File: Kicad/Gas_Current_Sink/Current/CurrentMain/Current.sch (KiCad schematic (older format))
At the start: 18 parts, among them J1 Vo's, J2 ACS770, J3 ACS712, J4 PA3208, J5 SCT, J6 Current

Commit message: Kicad Current project update Kicad TH project update
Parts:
- removed J2: ACS770, symbol CONN_01X05
- removed J3: ACS712, symbol CONN_01X05
- removed J6: Current, symbol CONN_01X02
- added J?: ACS770, symbol CONN_01X03
- added J?: ACS712, symbol CONN_01X03
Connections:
- net labels removed: IP+
- wire segments 58 -> 49
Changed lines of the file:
@@
-$EndComp
-$Comp
-L CONN_01X05 J2
-U 1 1 59DBFBDD
-P 1650 1200
-F 0 "J2" H 1650 1500 50  0000 C CNN
-F 1 "ACS770" V 1750 1200 50  0000 C CNN
-F 2 "" H 1650 1200 50  0001 C CNN
-F 3 "" H 1650 1200 50  0001 C CNN
-	1    1650 1200
-	0    -1   -1   0
 $EndComp
 $Comp
@@
 	1    900  2600
 	1    0    0    -1
-$EndComp
-$Comp
-L CONN_01X05 J3
-U 1 1 59DC12C8
-P 3550 1200
-F 0 "J3" H 3550 1500 50  0000 C CNN
-F 1 "ACS712" V 3650 1200 50  0000 C CNN
-F 2 "" H 3550 1200 50  0001 C CNN
-F 3 "" H 3550 1200 50  0001 C CNN
-	1    3550 1200
-	0    -1   -1   0
 $EndComp
 $Comp
@@
 $EndComp
 $Comp
-L CONN_01X02 J6
-U 1 1 59DC2BB0
-P 2550 2050
-F 0 "J6" H 2550 2200 50  0000 C CNN
-F 1 "Current" V 2650 2050 50  0000 C CNN
-F 2 "" H 2550 2050 50  0001 C CNN
-F 3 "" H 2550 2050 50  0001 C CNN
-	1    2550 2050
-	0    -1   -1   0
-$EndComp
-$Comp
 L R R?
 U 1 1 59DC56D2
@@
 Wire Wire Line
 	6000 1400 6100 1400
-Wire Wire Line
-	2500 2250 1750 2250
-Wire Wire Line
-	1750 2250 1750 1400
-Wire Wire Line
-	1750 1500 3650 1500
-Wire Wire Line
-	3650 1500 3650 1400
-Connection ~ 1750 1500
-Wire Wire Line
-	2600 2250 2600 2300
-Wire Wire Line
-	2600 2300 1850 2300
-Wire Wire Line
-	1850 2300 1850 1400
-Wire Wire Line
-	2550 2300 3750 2300
-Wire Wire Line
-	3750 2300 3750 1400
-Connection ~ 2550 2300
 Wire Wire Line
 	1550 1400 1550 2600
@@
 	650  1800 650  800
 Connection ~ 800  800
-Text Label 1750 1900 1    60   ~ 0
-IP+
 Wire Wire Line
 	6300 1700 6300 800
@@
 	6800 2200 6900 2200
 Connection ~ 6900 2200
+$Comp
+L CONN_01X03 J?
+U 1 1 59DD152B
+P 1550 1200
+F 0 "J?" H 1550 1400 50  0000 C CNN
+F 1 "ACS770" V 1650 1200 50  0000 C CNN
+F 2 "" H 1550 1200 50  0001 C CNN
+F 3 "" H 1550 1200 50  0001 C CNN
+	1    1550 1200
+	0    -1   -1   0
+$EndComp
+$Comp
+L CONN_01X03 J?
+U 1 1 59DD16D9
+P 3450 1200
+F 0 "J?" H 3450 1400 50  0000 C CNN
+F 1 "ACS712" V 3550 1200 50  0000 C CNN
+F 2 "" H 3450 1200 50  0001 C CNN
+F 3 "" H 3450 1200 50  0001 C CNN
+	1    3450 1200
+	0    -1   -1   0
+$EndComp
 $EndSCHEMATC

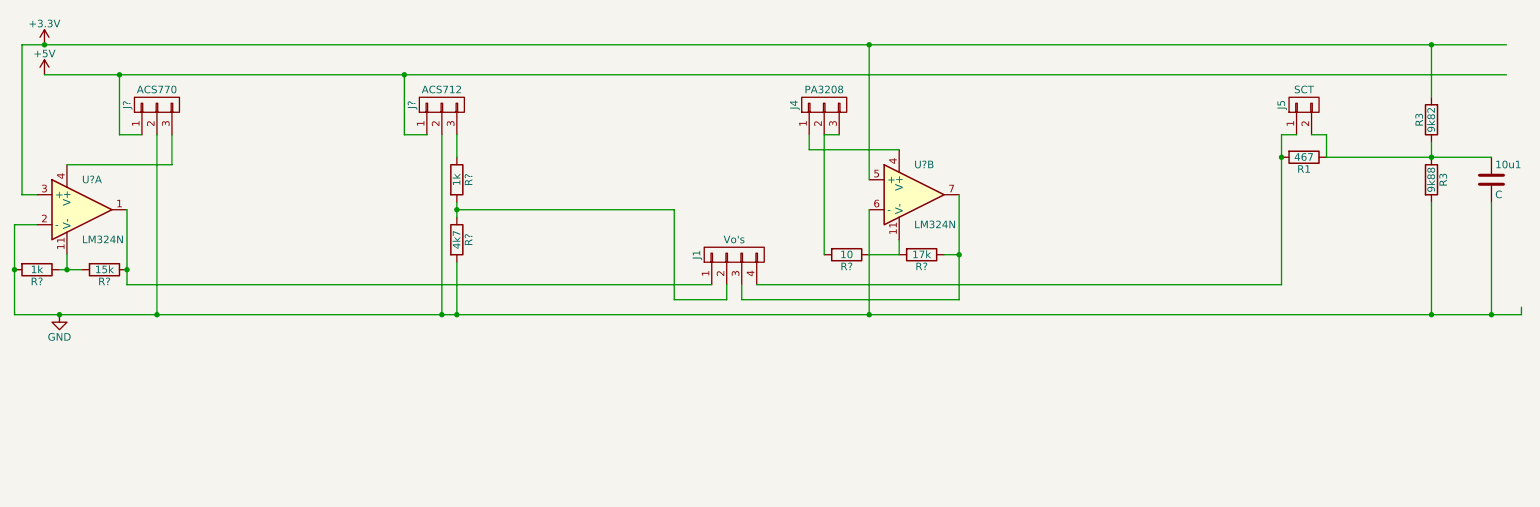
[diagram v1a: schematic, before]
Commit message: Update to schematic and pcb almost complete (drill holes missing)
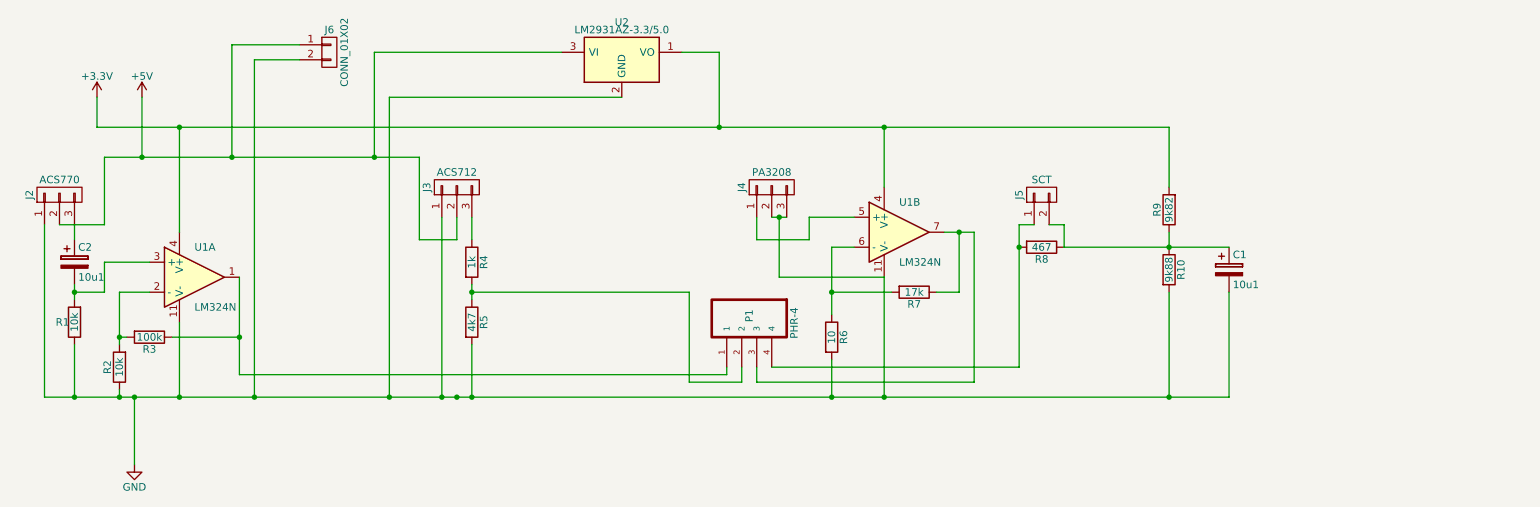
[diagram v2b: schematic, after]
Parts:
- removed 10u1: C, symbol C
- removed J1: Vo's, symbol CONN_01X04
- added C1, C2: 10u1, Capacitors_THT:CP_Radial_D5.0mm_P2.50mm, symbol CP
- added J6: CONN_01X02, Connectors_Molex:Molex_KK-6410-02_02x2.54mm_Straight, symbol CONN_01X02
- added P1: PHR-4, ecoPlanos_custom:JST_PHR-4, symbol PHR-4
- added R1: 10k, Resistors_THT:R_Axial_DIN0207_L6.3mm_D2.5mm_P7.62mm_Horizontal, symbol R
- added U2: LM2931AZ-3.3/5.0, TO_SOT_Packages_THT:TO-220_Vertical, symbol LM2931AZ-3.3/5.0
- J2, J3: renamed from J?; footprint (none) -> Pin_Headers:Pin_Header_Straight_1x03_Pitch2.54mm
- J4: footprint (none) -> Pin_Headers:Pin_Header_Straight_1x03_Pitch2.54mm
- J5: footprint (none) -> Pin_Headers:Pin_Header_Straight_1x02_Pitch2.54mm
- R10, R9: renamed from R3; footprint (none) -> Resistors_THT:R_Axial_DIN0207_L6.3mm_D2.5mm_P7.62mm_Horizontal
- R2: renamed from R?; value 1k -> 10k; footprint (none) -> Resistors_THT:R_Axial_DIN0207_L6.3mm_D2.5mm_P7.62mm_Horizontal
- R3: renamed from R?; value 15k -> 100k; footprint (none) -> Resistors_THT:R_Axial_DIN0207_L6.3mm_D2.5mm_P7.62mm_Horizontal
- R4, R5, R6, R7: renamed from R?; footprint (none) -> Resistors_THT:R_Axial_DIN0207_L6.3mm_D2.5mm_P7.62mm_Horizontal
- R8: renamed from R1; footprint (none) -> Resistors_THT:R_Axial_DIN0207_L6.3mm_D2.5mm_P7.62mm_Horizontal
- U1: renamed from U?; footprint (none) -> Housings_DIP:DIP-14_W7.62mm
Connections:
- wire segments 49 -> 75
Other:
- moved on the sheet: J2, J3, J4, J5, R10, R2, R3, R4, R5, R6, R7, R8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

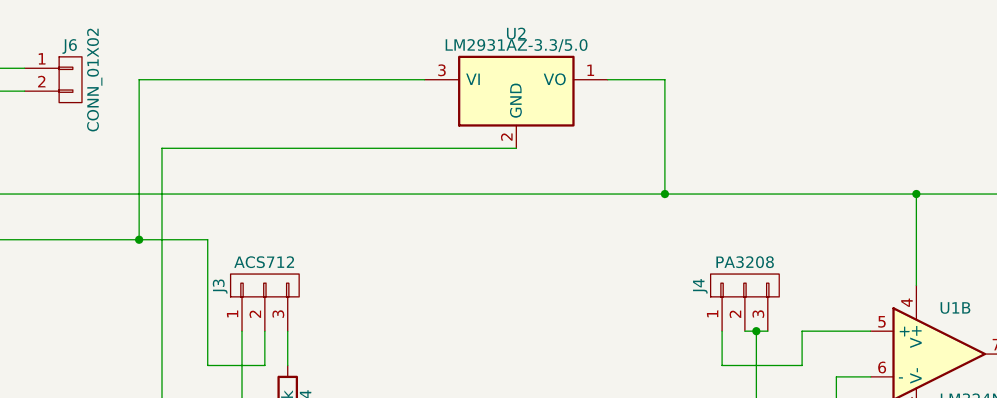
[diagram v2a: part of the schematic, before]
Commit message: Minor changes on pcb routing.
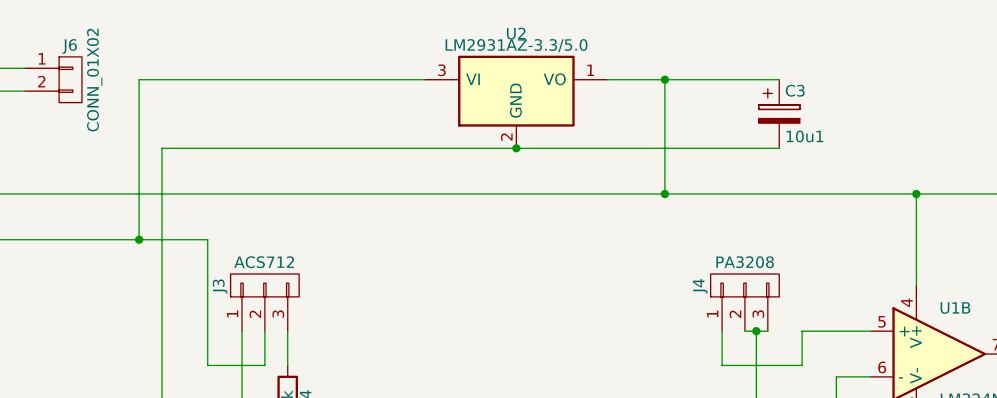
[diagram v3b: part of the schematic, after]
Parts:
- added C3: 10u1, Capacitors_THT:CP_Radial_Tantal_D9.0mm_P5.00mm, symbol CP
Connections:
- net +3V3: now also C3.1
- net GND: now also C3.2
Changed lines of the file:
@@
+	1    0    0    -1
+$EndComp
+$Comp
+L CP C3
+U 1 1 59E88507
+P 5800 1000
+F 0 "C3" H 5825 1100 50  0000 L CNN
+F 1 "10u1" H 5825 900 50  0000 L CNN
+F 2 "Capacitors_THT:CP_Radial_Tantal_D9.0mm_P5.00mm" H 5838 850 50  0001 C CNN
+F 3 "" H 5800 1000 50  0001 C CNN
+	1    5800 1000
 	1    0    0    -1
 $EndComp
@@
 	5300 1350 5300 850
 Wire Wire Line
-	5300 850  5050 850
+	5050 850  5800 850
 Wire Wire Line
 	3000 850  3000 1550
@@
 	3100 1150 3100 3150
 Wire Wire Line
-	4650 1150 3100 1150
+	3100 1150 5800 1150
 Connection ~ 2050 1550
 Wire Wire Line
@@
 	3300 2100 3300 1550
 Connection ~ 3000 1550
+Connection ~ 5300 850
+Connection ~ 4650 1150
 $EndSCHEMATC

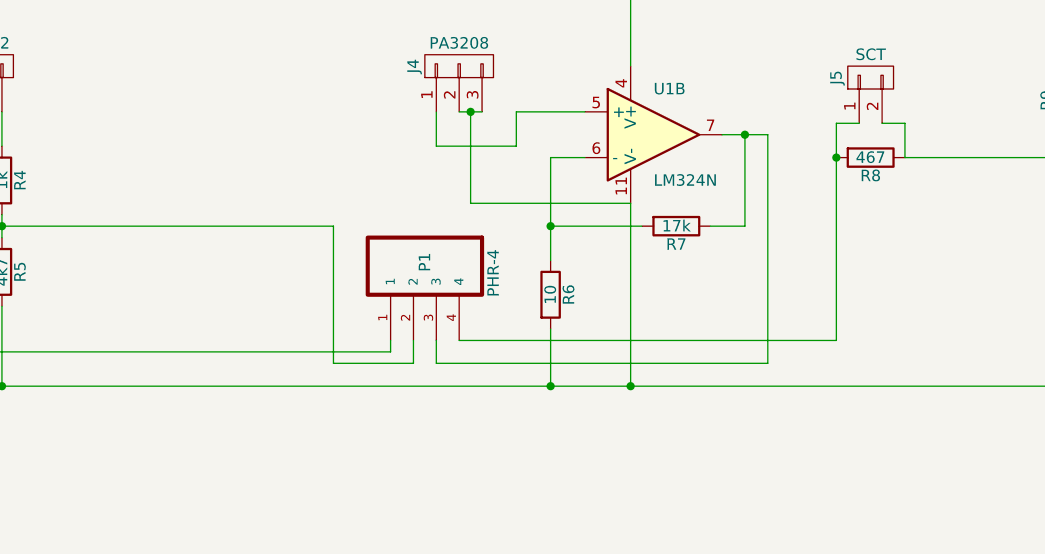
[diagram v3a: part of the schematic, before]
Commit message: Added some lables to schematic.
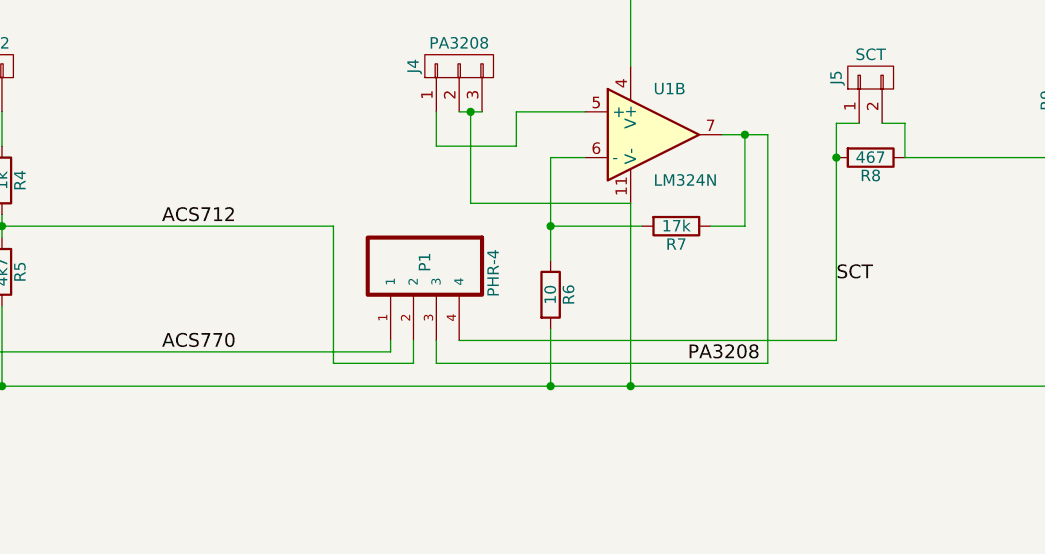
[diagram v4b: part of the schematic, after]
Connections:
- net SCT: now reaches J5.1 (P1), P1.4, R8.2
- net ACS712: now reaches P1.2, R4.2, R5.1
- net ACS770: now reaches P1.1, R3.1, U1.1
- net PA3208: now reaches P1.3, R7.1, U1.7
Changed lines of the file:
@@
 EESchema Schematic File Version 2
-LIBS:ecoPlanos_custom
 LIBS:power
 LIBS:device
@@
 LIBS:valves
 LIBS:Common-Parts-Library
-LIBS:freetronics_schematic
 LIBS:Current-cache
 EELAYER 25 0
@@
 Connection ~ 5300 850
 Connection ~ 4650 1150
+Text Label 4350 3000 0    60   ~ 0
+ACS770
+Text Label 4350 2450 0    60   ~ 0
+ACS712
+Text Label 6650 3050 0    60   ~ 0
+PA3208
+Text Label 7300 2700 0    60   ~ 0
+SCT
 $EndSCHEMATC
